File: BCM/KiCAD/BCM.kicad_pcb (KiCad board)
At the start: 2 copper layers, 150 x 99.1 mm, 153 parts, among them J10 Back_9, J11 Back_10, J12 Back_11, J13 Back_12, J14 Eye1, J15 Eye2, J16 Nose, J17 S1, J18 S2, J19 S3, J2 Back_1, J20 S4, J21 S5, J22 Door2, J23 Door1, J24 But1, J25 But2, J26 But3, J27 But4, J28 But5, J29 But6, J3 Back_2, J4 Back_3, J5 Back_4, J6 Back_5, J7 Back_6, J8 Back_7, J9 Back_8, Q1 2N7002, Q10 2N7002, Q11 2N7002, Q12 2N7002, Q13 2N7002, Q14 2N7002, Q15 2N7002, Q16 2N7002, Q17 2N7002, Q18 2N7002, Q19 2N7002, Q2 2N7002, Q20 2N7002, Q3 2N7002, Q4 2N7002, Q5 2N7002, Q6 2N7002, Q7 2N7002, Q8 2N7002, Q9 2N7002, U1 TPS54331D

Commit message: updates
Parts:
- added J30: Power, Connector_JST:JST_XA_B06B-XASK-1_1x06_P2.50mm_Vertical, B.Cu at (61.0, 124.5)
- added R81: 29.4k, Resistor_SMD:R_0805_2012Metric_Pad1.20x1.40mm_HandSolder, F.Cu at (74.6, 69.7)
- added R82: 10k2, Resistor_SMD:R_0805_2012Metric_Pad1.20x1.40mm_HandSolder, F.Cu at (74.6, 72.6)
- added R83: 1k96, Resistor_SMD:R_0805_2012Metric_Pad1.20x1.40mm_HandSolder, F.Cu at (74.6, 75.6)
- moved D3 196.9 mm to (47.6, 119.4), turned to 180 degrees
- moved R84 196.2 mm to (47.6, 116.8)
- moved F1 182.8 mm to (58.4, 108.0)
- moved D1 175.5 mm to (56.5, 114.9), turned to -90 degrees
- moved C16 170.5 mm to (70.1, 45.6)
- moved C17 170.5 mm to (70.1, 52.4)
- moved C9 170.5 mm to (70.1, 38.7)
- moved U1 170.5 mm to (80.0, 59.2)
- moved C10 170.5 mm to (77.0, 36.8)
- moved C11 170.5 mm to (77.0, 39.8)
- moved C12 170.5 mm to (77.0, 42.8)
- moved C13 170.5 mm to (77.0, 45.8)
- moved C14 170.5 mm to (77.0, 48.9)
- moved C15 170.5 mm to (77.0, 51.9)
- moved D4 158.3 mm to (60.3, 114.9), turned to -90 degrees
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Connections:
- C10 pad 1: Vin+Ve -> Vin+Ve (fused)
- C9 pad 1: Vin+Ve -> Vin+Ve (fused)
- D1 pad 1: Net-(D1-K) -> Vin+Ve
- D4 pad 1: Net-(D1-K) -> Vin+Ve
- F1 pad 1: Vin+Ve -> Vin+Ve (fused)
- F1 pad 2: Net-(D1-K) -> Vin+Ve
- U1 pad 2: Vin+Ve -> Vin+Ve (fused)
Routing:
- net GND: track 94.9 -> 100.1 mm
- net Net-(D3-A): track 0.00 -> 2.55 mm
- net Vin+Ve: track 0.00 -> 0.61 mm
- added copper zone on F.Cu, net +BATT
- added copper zone on F.Cu, net +VDC
- added copper zone on F.Cu, net Vin+Ve

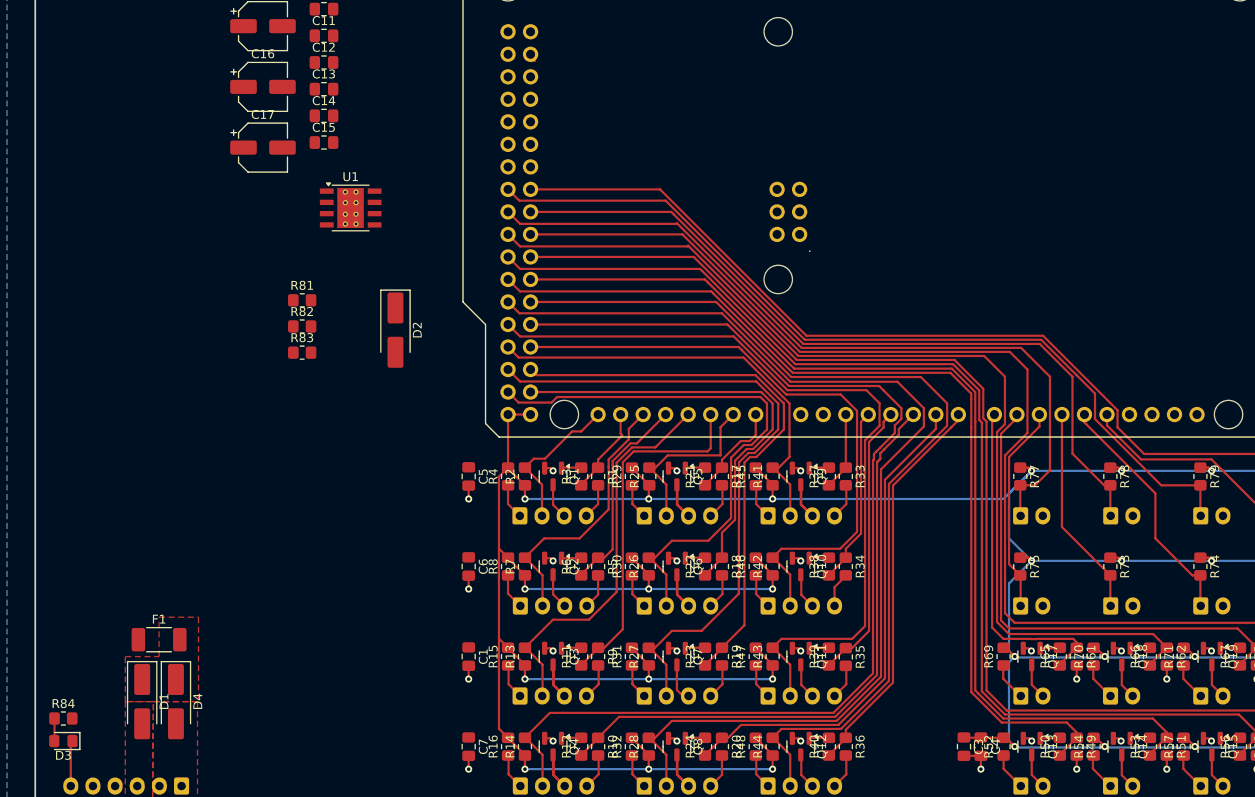
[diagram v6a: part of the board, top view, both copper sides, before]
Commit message: SDA SCL recovered
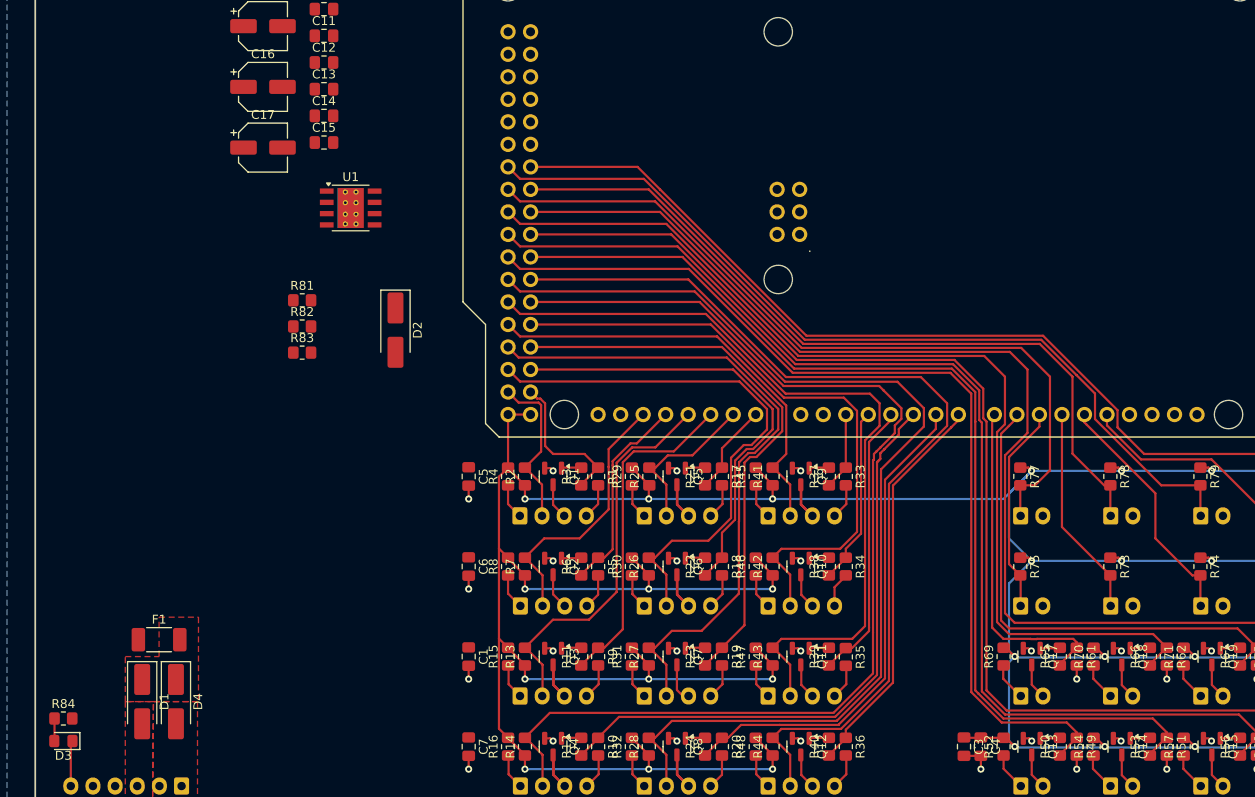
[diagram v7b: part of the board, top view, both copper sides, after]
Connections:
- XA1 pad D20: /Back Button Connectors/BackLED1 -> unconnected-(XA1-D20_SDA-PadD20)
- XA1 pad D21: /Back Button Connectors/BackButton1 -> unconnected-(XA1-D21_SCL-PadD21)
- XA1 pad D22: /Back Button Connectors/BackLED6 -> /Back Button Connectors/BackLED1
- XA1 pad D23: /Back Button Connectors/BackButton6 -> /Back Button Connectors/BackButton1
- XA1 pad D24: /Back Button Connectors/BackLED7 -> /Back Button Connectors/BackLED6
- XA1 pad D25: /Back Button Connectors/BackButton7 -> /Back Button Connectors/BackButton6
- XA1 pad D26: /Back Button Connectors/BackButton10 -> /Back Button Connectors/BackLED7
- XA1 pad D27: /Back Button Connectors/BackButton9 -> /Back Button Connectors/BackButton7
- XA1 pad D28: /Back Button Connectors/BackButton4 -> /Back Button Connectors/BackButton10
- XA1 pad D29: /Back Button Connectors/BackButton11 -> /Back Button Connectors/BackButton9
- XA1 pad D30: /Back Button Connectors/BackButton12 -> /Back Button Connectors/BackButton4
- XA1 pad D31: /Back Button Connectors/BackButton8 -> /Back Button Connectors/BackButton11
- XA1 pad D32: /Misc Lights/EyesLight2 -> /Back Button Connectors/BackButton12
- XA1 pad D33: /Misc Lights/EyesLight1 -> /Back Button Connectors/BackButton8
- XA1 pad D34: /Misc Lights/SpaireLight1 -> /Misc Lights/EyesLight2
- XA1 pad D35: /Misc Lights/NoseLight -> /Misc Lights/EyesLight1
- XA1 pad D36: /Misc Lights/SpaireLight5 -> /Misc Lights/SpaireLight1
- XA1 pad D37: /Misc Lights/SpaireLight3 -> /Misc Lights/NoseLight
- XA1 pad D38: /Misc Switches/SpaireBut4 -> /Misc Lights/SpaireLight5
- XA1 pad D39: /Misc Switches/SpaireBut3 -> /Misc Lights/SpaireLight3
- XA1 pad D40: /Misc Switches/SpaireBut6 -> /Misc Switches/SpaireBut4
- XA1 pad D41: /Misc Switches/SpaireBut5 -> /Misc Switches/SpaireBut3
- XA1 pad D42: unconnected-(XA1-PadD42) -> /Misc Switches/SpaireBut6
- XA1 pad D43: unconnected-(XA1-PadD43) -> /Misc Switches/SpaireBut5
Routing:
- net /Back Button Connectors/BackLED1: track 9.88 -> 16.7 mm
- net /Back Button Connectors/BackLED3: track 39.6 -> 37.3 mm
- net /Back Button Connectors/BackButton5: track 20.0 -> 18.2 mm
- net /Back Button Connectors/BackButton1: track 17.0 -> 18.4 mm
- net unconnected-(XA1-PadD52): track 1.26 -> 0.00 mm
- net /Misc Lights/SpaireLight1: track 137.3 -> 138.4 mm
- net /Misc Lights/EyesLight2: track 116.0 -> 117.0 mm
- net /Back Button Connectors/BackButton8: track 119.5 -> 120.5 mm
- net /Back Button Connectors/BackButton4: track 125.5 -> 126.6 mm
- net /Back Button Connectors/BackButton10: track 70.4 -> 71.5 mm
- net /Misc Switches/SpaireBut6: track 104.1 -> 105.1 mm
- net /Misc Switches/SpaireBut5: track 97.0 -> 98.1 mm
- net /Misc Switches/SpaireBut4: track 86.7 -> 87.7 mm
- net /Misc Lights/SpaireLight5: track 133.8 -> 134.8 mm
- net /Misc Lights/NoseLight: track 129.7 -> 130.8 mm
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
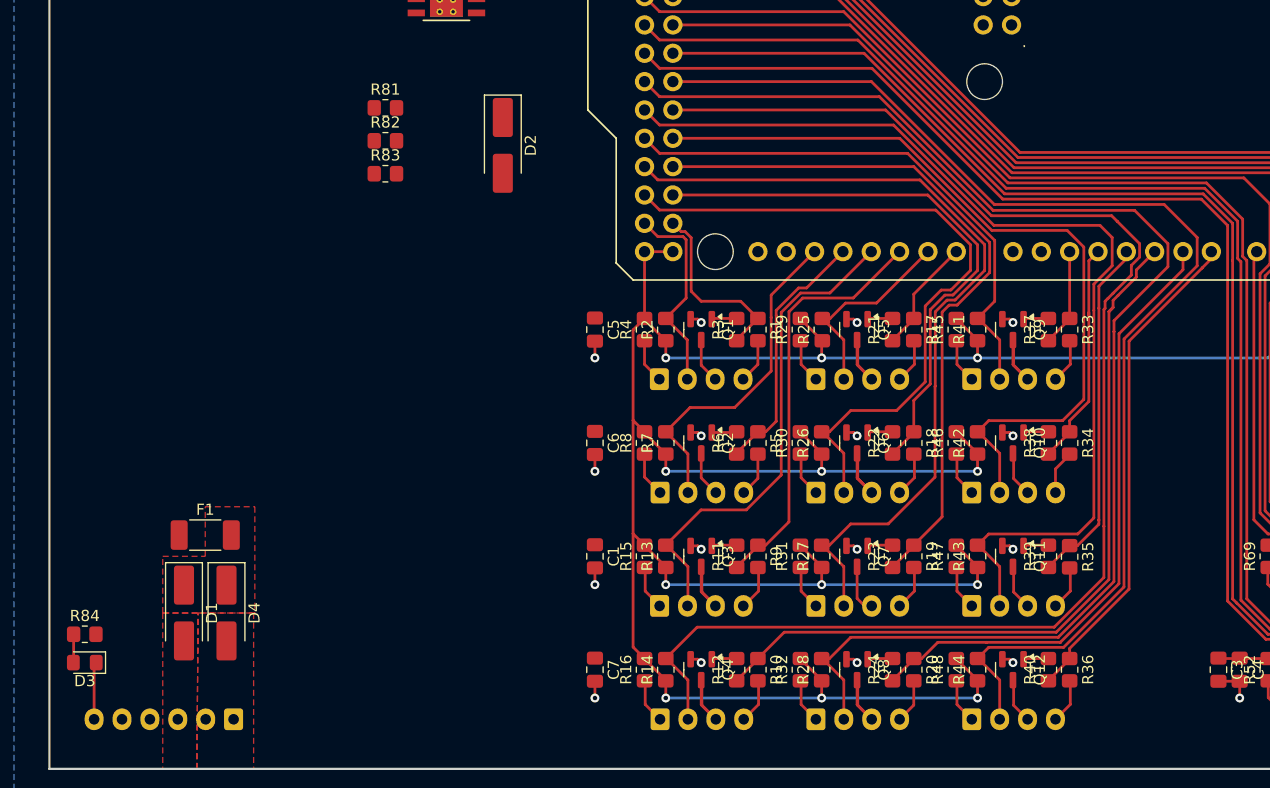
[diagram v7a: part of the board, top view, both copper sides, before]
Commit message: added servos
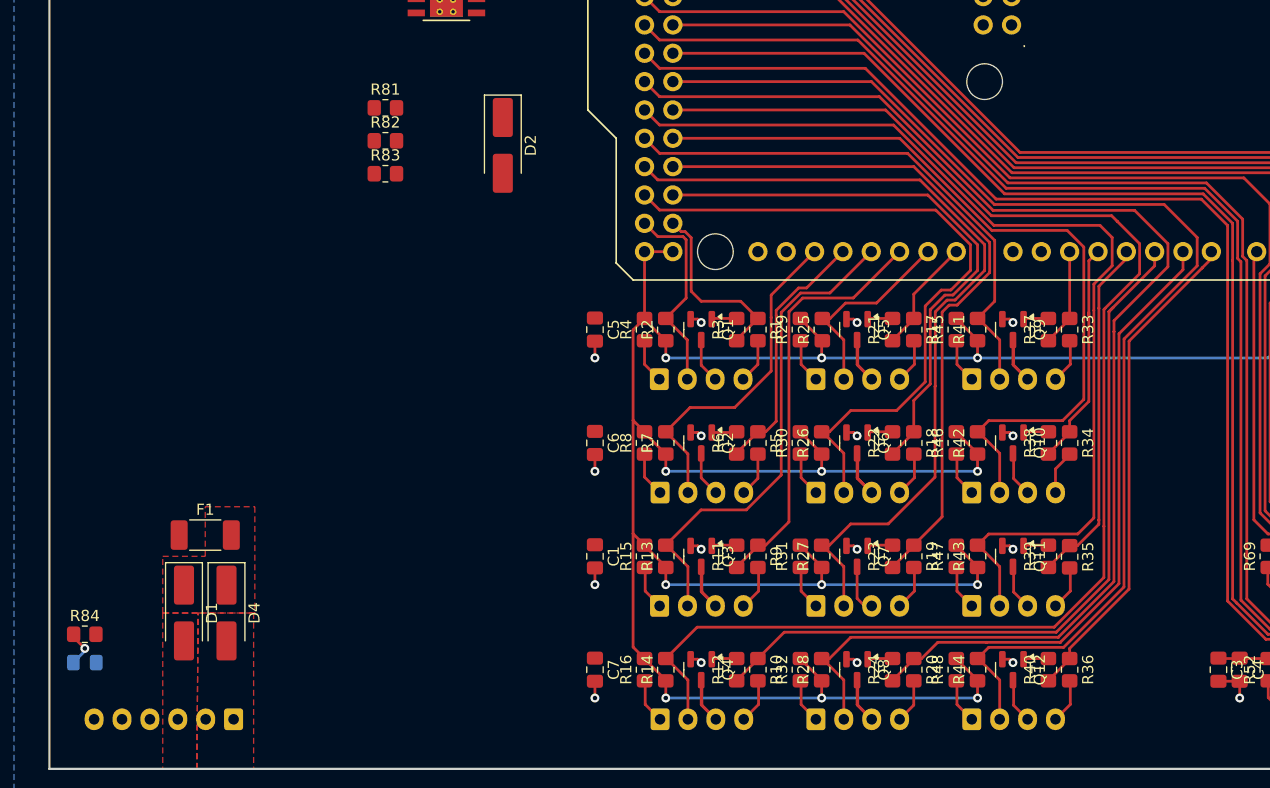
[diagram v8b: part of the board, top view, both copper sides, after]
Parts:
- D3: moved to B.Cu
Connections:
- XA1 pad D44: unconnected-(XA1-PadD44) -> /Shrimp/SpairServo1
- XA1 pad D45: unconnected-(XA1-PadD45) -> /Shrimp/SpairServo2
- XA1 pad D46: unconnected-(XA1-PadD46) -> /Shrimp/SpairServo3
- XA1 pad D47: unconnected-(XA1-PadD47) -> /Shrimp/TailServo1
- XA1 pad D48: unconnected-(XA1-PadD48) -> /Shrimp/TailServo2
- XA1 pad D49: unconnected-(XA1-PadD49) -> /Shrimp/NeckServo
- XA1 pad D50: unconnected-(XA1-PadD50) -> /Shrimp/EarServo1
- XA1 pad D51: unconnected-(XA1-PadD51) -> /Shrimp/EarServo2
- XA1 pad D52: unconnected-(XA1-PadD52) -> /Shrimp/NoseServo1
- XA1 pad D53: unconnected-(XA1-D53_SS-PadD53) -> /Shrimp/NoseServo2
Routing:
- net GND: track 99.8 -> 94.9 mm
- net Net-(D3-A): track 2.52 -> 3.38 mm, vias 0 -> 1
